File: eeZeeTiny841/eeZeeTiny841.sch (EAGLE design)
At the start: 12 parts, among them IC1 ATtiny841, J2 avrisp, Q1 16MHz

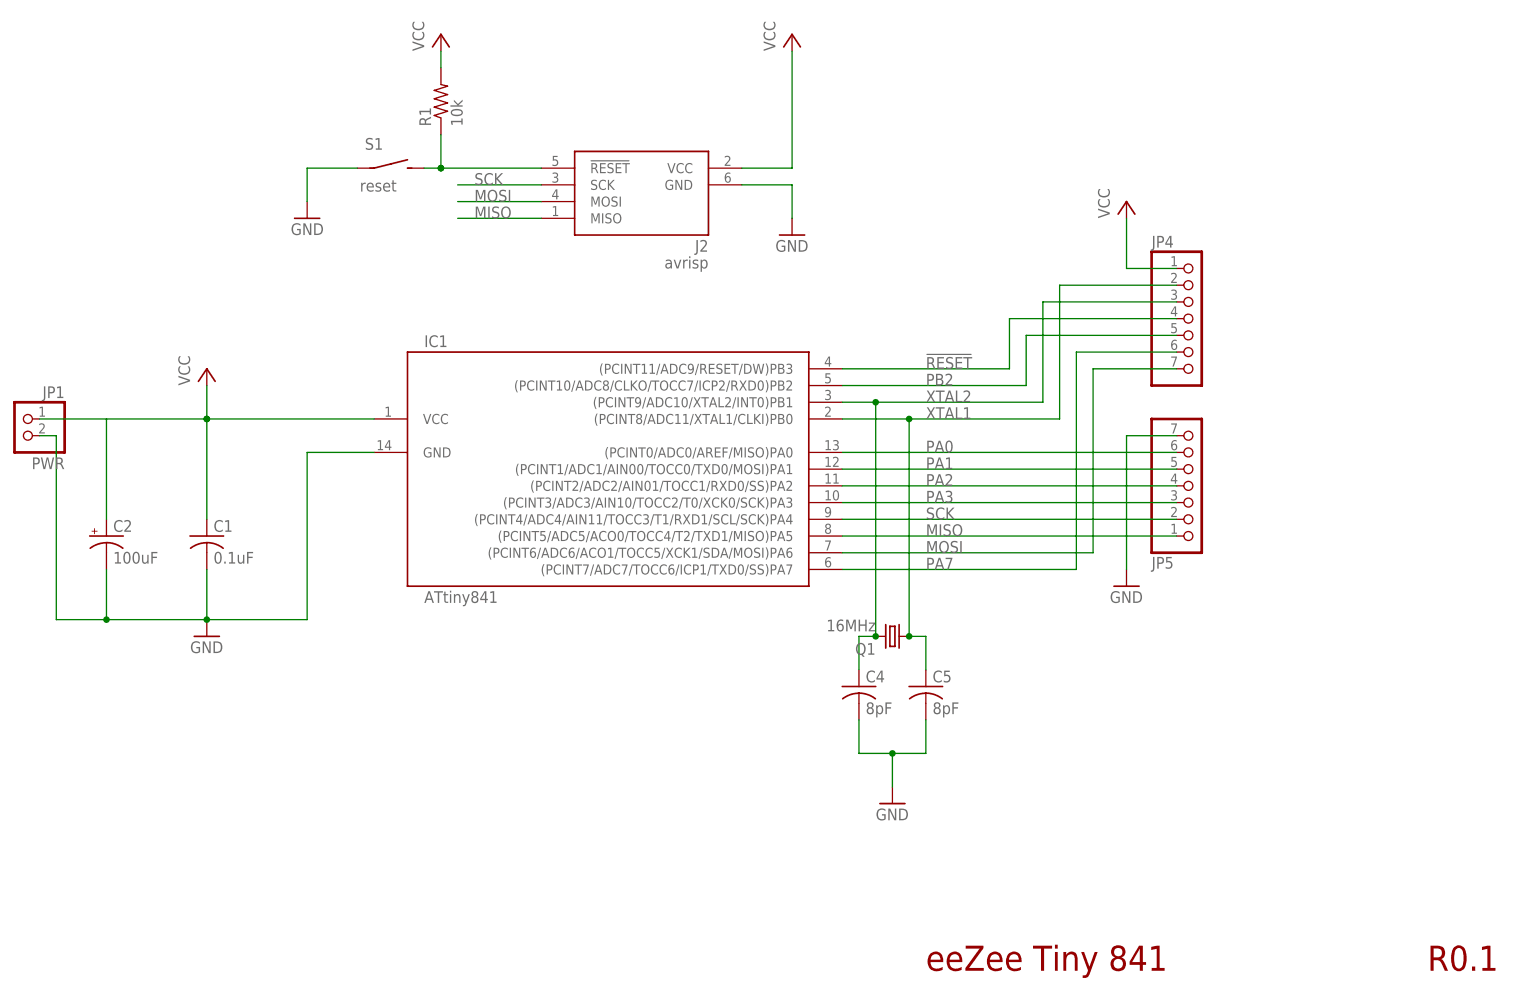
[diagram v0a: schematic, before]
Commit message: Minor mods to board/schematic. avrdude config from AVRfreaks forum.
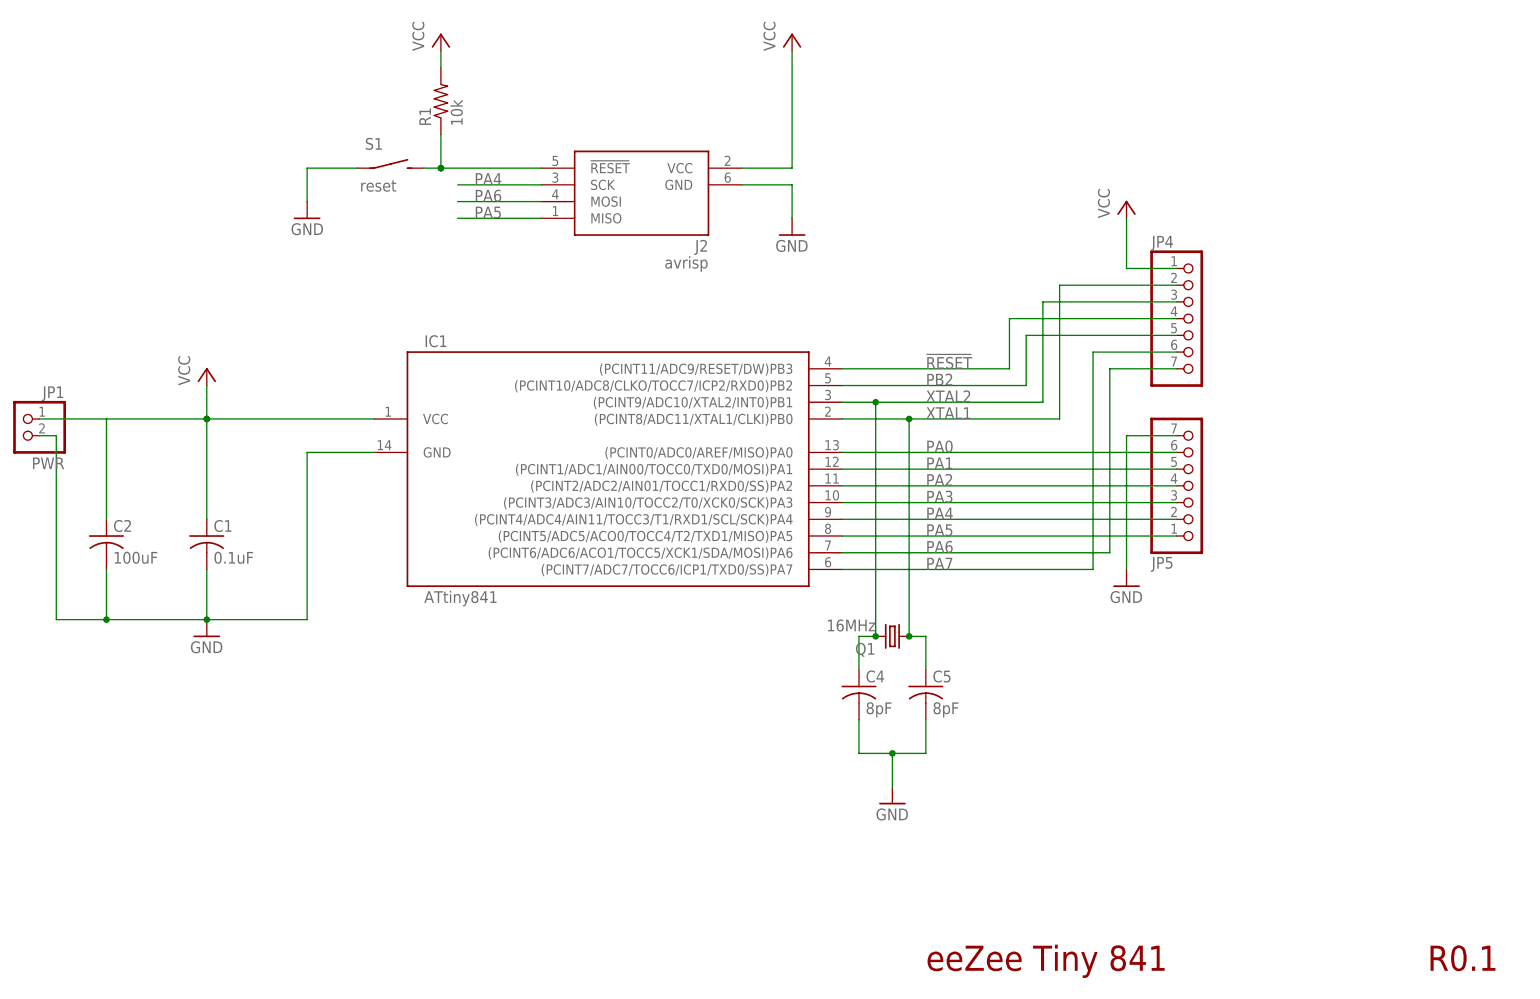
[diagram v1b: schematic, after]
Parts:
- C2: device mes_rcl:CAP_POL_SMC_B -> rcl:C-USC1206
- J2: device bt_avr:AVRISP6 -> bt_avr:AVRISP6_COMPACT
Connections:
- net SCK renamed PA4
- removed net MISO: IC1.(PCINT2/ADC2/AIN01/TOCC1/RXD0/SS)PA2, J2.MISO, JP5.4
- removed net MOSI: IC1.(PCINT1/ADC1/AIN00/TOCC0/TXD0/MOSI)PA1, J2.MOSI, JP5.5
- new net PA5: IC1.(PCINT5/ADC5/ACO0/TOCC4/T2/TXD1/MISO)PA5, J2.MISO, JP5.1
- new net PA6: IC1.(PCINT6/ADC6/ACO1/TOCC5/XCK1/SDA/MOSI)PA6, J2.MOSI, JP4.7
- net GND: now also C2.2; no longer C2.-
- net PA0: now also IC1.(PCINT0/ADC0/AREF/MISO)PA0, JP5.6; no longer IC1.(PCINT7/ADC7/TOCC6/ICP1/TXD0/SS)PA7, JP4.6
- net PA1: now also IC1.(PCINT1/ADC1/AIN00/TOCC0/TXD0/MOSI)PA1, JP5.5; no longer IC1.(PCINT6/ADC6/ACO1/TOCC5/XCK1/SDA/MOSI)PA6, JP4.7
- net PA2: now also IC1.(PCINT2/ADC2/AIN01/TOCC1/RXD0/SS)PA2, JP5.4; no longer IC1.(PCINT5/ADC5/ACO0/TOCC4/T2/TXD1/MISO)PA5, JP5.1
- net PA7: now also IC1.(PCINT7/ADC7/TOCC6/ICP1/TXD0/SS)PA7, JP4.6; no longer IC1.(PCINT0/ADC0/AREF/MISO)PA0, JP5.6
- net VCC: now also C2.1; no longer C2.+
